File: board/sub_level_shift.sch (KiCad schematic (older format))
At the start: 17 parts, among them Q1501 Q_NPN_BEC, Q1502 Q_NPN_BEC, Q1503 Q_NPN_BEC, U1406 74LVC4245A, U1407 74LVC4245A, U1501 74LVC4245A, U1502 74LVC4245A, U1503 74LVC4245A, U1504 74LVC4245A, U1505 74LVC4245A

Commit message: More Schematic progress
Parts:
- added C1401, C1402, C1403, C1404, C1405, C1406, C1407: 1u, symbol Device:C
- renumbered Q1501 to Q1401, Q1502 to Q1402, Q1503 to Q1403, R1501 to R1401, R1502 to R1402, R1503 to R1403, R1504 to R1404, R1505 to R1405, R1506 to R1406, R1507 to R1407, U1406 to U1401, U1407 to U1402, U1501 to U1403, U1502 to U1404, U1503 to U1405, U1504 to U1406, U1505 to U1407
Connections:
- net +5V: now also C1401.1, C1402.1, C1403.1, C1404.1, C1405.1, C1406.1, C1407.1
- net A0: now also U1402.10 (A7), U1402.14 (B7); no longer U1401.21 (B0), U1401.3 (A0)
- net A1: now also U1402.15 (B6), U1402.9 (A6); no longer U1401.20 (B1), U1401.4 (A1)
- net A10: now also U1401.16 (B5), U1401.8 (A5); no longer U1402.19 (B2), U1402.5 (A2)
- net A11: now also U1401.17 (B4), U1401.7 (A4); no longer U1402.18 (B3), U1402.6 (A3)
- net A12: now also U1401.18 (B3), U1401.6 (A3); no longer U1402.17 (B4), U1402.7 (A4)
- net A13: now also U1401.19 (B2), U1401.5 (A2); no longer U1402.16 (B5), U1402.8 (A5)
- net A14: now also U1401.20 (B1), U1401.4 (A1); no longer U1402.15 (B6), U1402.9 (A6)
- net A15: now also U1401.21 (B0), U1401.3 (A0); no longer U1402.10 (A7), U1402.14 (B7)
- net A2: now also U1402.16 (B5), U1402.8 (A5); no longer U1401.19 (B2), U1401.5 (A2)
- net A3: now also U1402.17 (B4), U1402.7 (A4); no longer U1401.18 (B3), U1401.6 (A3)
- net A4: now also U1402.18 (B3), U1402.6 (A3); no longer U1401.17 (B4), U1401.7 (A4)
- net A5: now also U1402.19 (B2), U1402.5 (A2); no longer U1401.16 (B5), U1401.8 (A5)
- net A6: now also U1402.20 (B1), U1402.4 (A1); no longer U1401.15 (B6), U1401.9 (A6)
- net A7: now also U1402.21 (B0), U1402.3 (A0); no longer U1401.10 (A7), U1401.14 (B7)
- net A8: now also U1401.10 (A7), U1401.14 (B7); no longer U1402.21 (B0), U1402.3 (A0)
- net A9: now also U1401.15 (B6), U1401.9 (A6); no longer U1402.20 (B1), U1402.4 (A1)
- net GND: now also C1401.2, C1402.2, C1403.2, C1404.2, C1405.2, C1406.2, C1407.2
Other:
- moved on the sheet: Q1401, Q1402, Q1403, R1401, R1402, R1403, R1404, R1405, R1406, R1407, U1401, U1402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

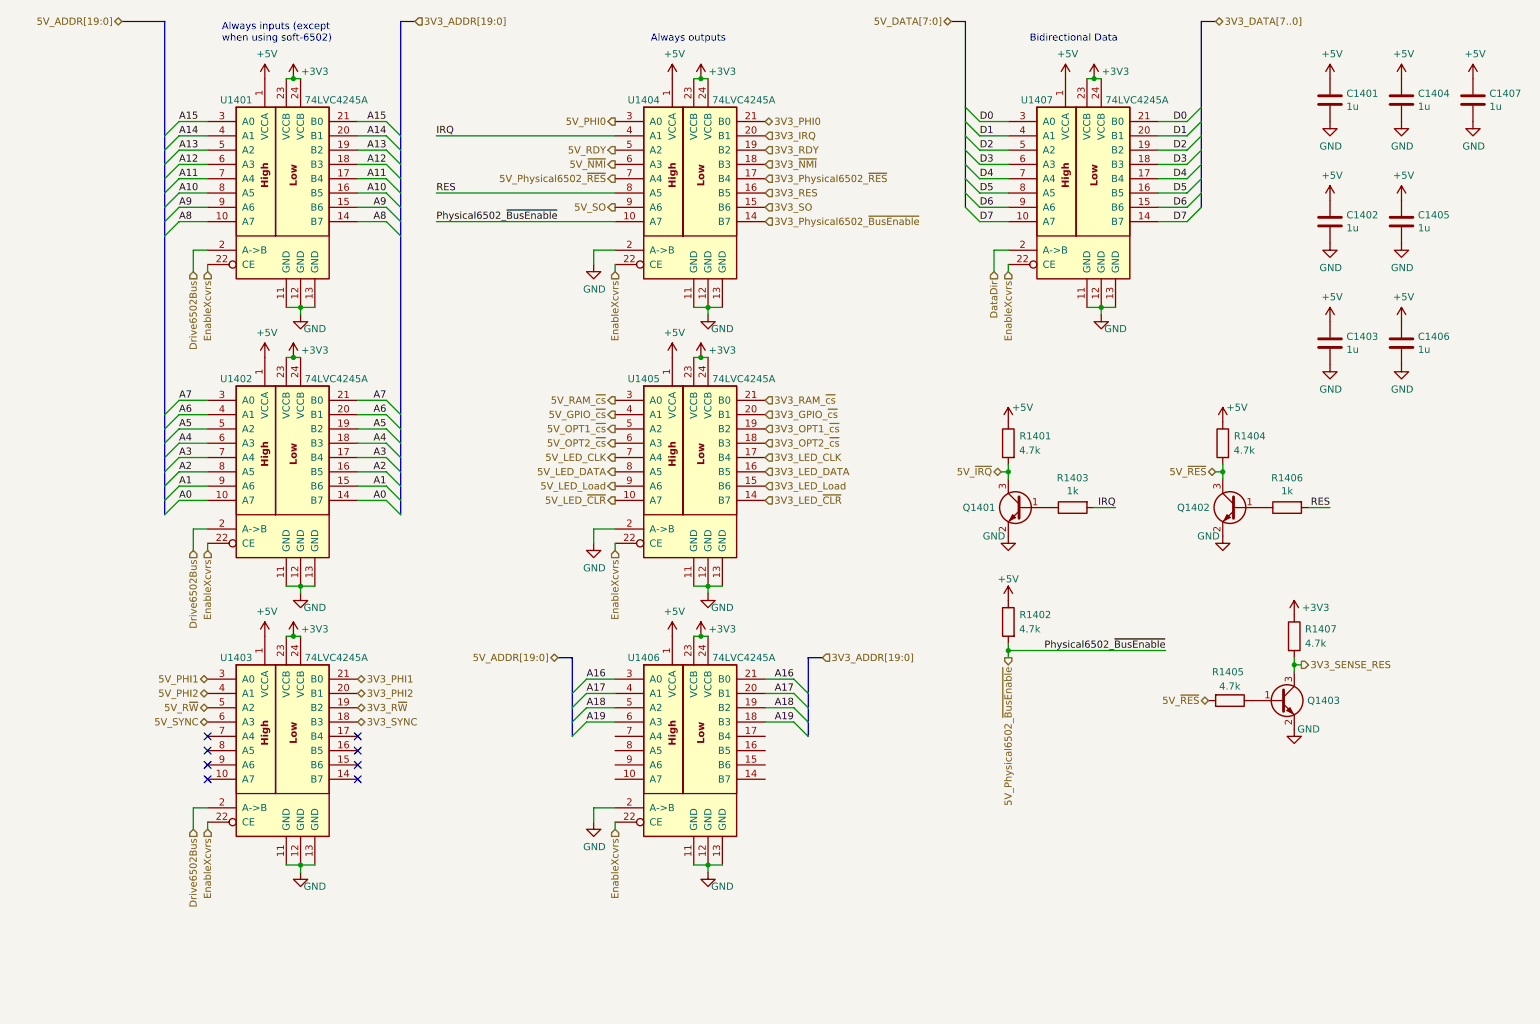
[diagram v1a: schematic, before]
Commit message: Bus signal connectivity rebuilt
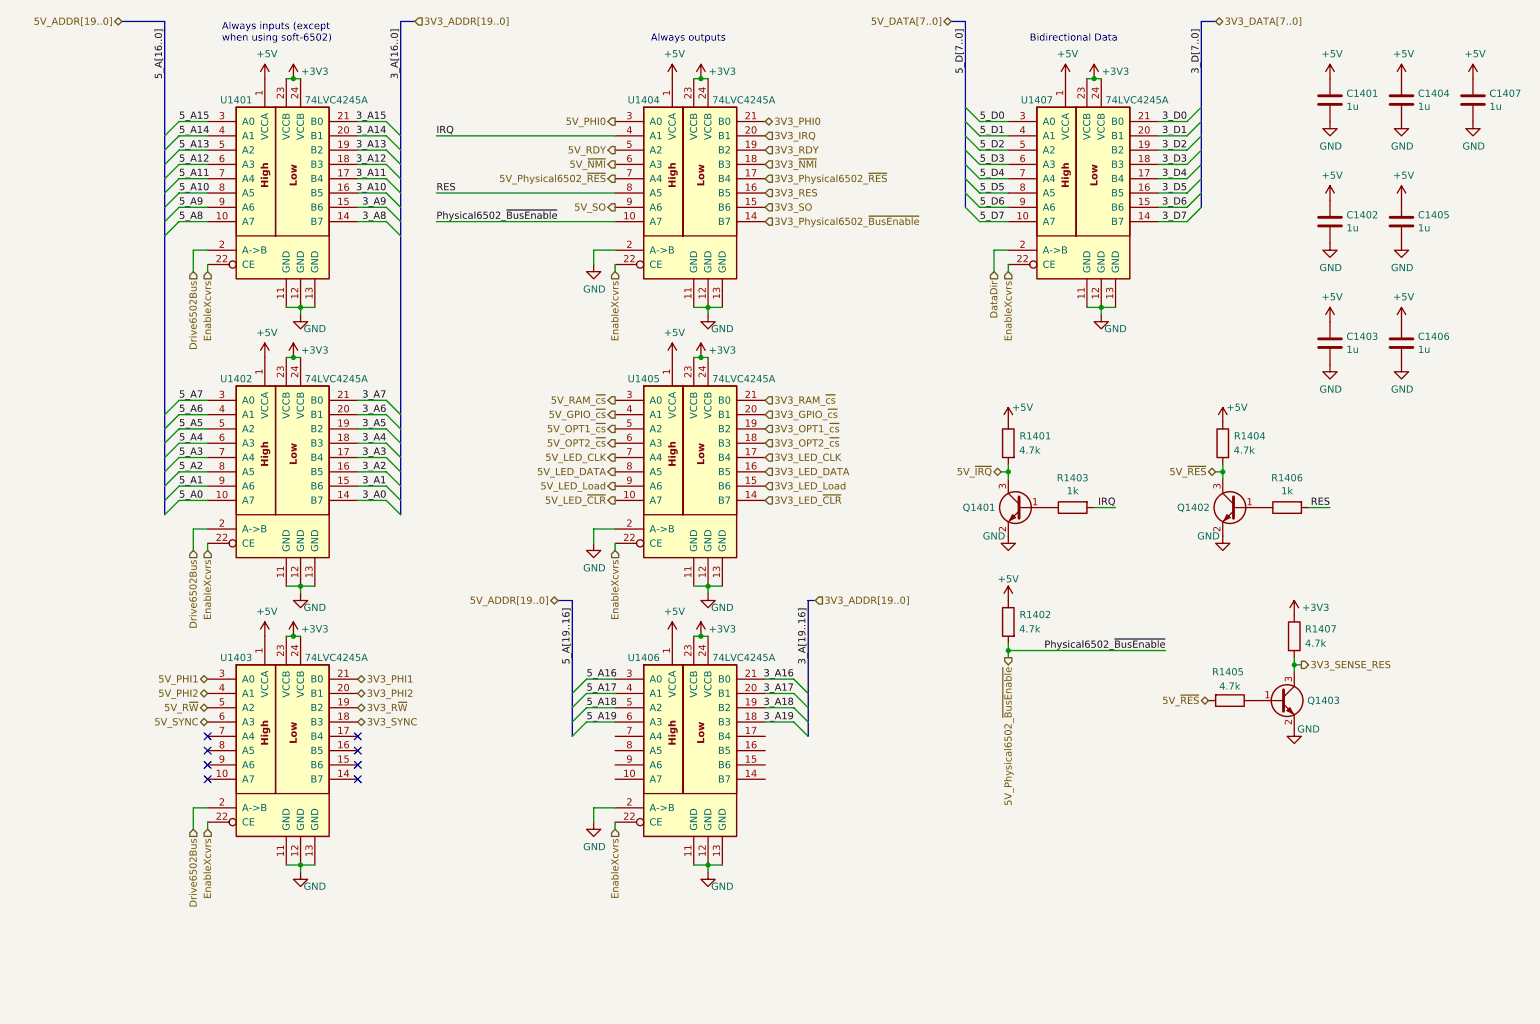
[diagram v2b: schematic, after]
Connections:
- net A0 renamed 3_A0
- net 3_A0: no longer U1402.10 (A7)
- net A1 renamed 3_A1
- net 3_A1: no longer U1402.9 (A6)
- net A10 renamed 3_A10
- net 3_A10: no longer U1401.8 (A5)
- net A11 renamed 3_A11
- net 3_A11: no longer U1401.7 (A4)
- net A12 renamed 3_A12
- net 3_A12: no longer U1401.6 (A3)
- net A13 renamed 3_A13
- net 3_A13: no longer U1401.5 (A2)
- net A14 renamed 3_A14
- net 3_A14: no longer U1401.4 (A1)
- net A15 renamed 3_A15
- net 3_A15: no longer U1401.3 (A0)
- net A16 renamed 3_A16
- net 3_A16: no longer U1406.3 (A0)
- net A17 renamed 3_A17
- net 3_A17: no longer U1406.4 (A1)
- net A18 renamed 3_A18
- net 3_A18: no longer U1406.5 (A2)
- net A19 renamed 3_A19
- net 3_A19: no longer U1406.6 (A3)
- net A2 renamed 3_A2
- net 3_A2: no longer U1402.8 (A5)
- net A3 renamed 3_A3
- net 3_A3: no longer U1402.7 (A4)
- net A4 renamed 3_A4
- net 3_A4: no longer U1402.6 (A3)
- net A5 renamed 3_A5
- net 3_A5: no longer U1402.5 (A2)
- net A6 renamed 3_A6
- net 3_A6: no longer U1402.4 (A1)
- net A7 renamed 3_A7
- net 3_A7: no longer U1402.3 (A0)
- net A8 renamed 3_A8
- net 3_A8: no longer U1401.10 (A7)
- net A9 renamed 3_A9
- net 3_A9: no longer U1401.9 (A6)
- net D0 renamed 3_D0
- net 3_D0: no longer U1407.3 (A0)
- net D1 renamed 3_D1
- net 3_D1: no longer U1407.4 (A1)
- net D2 renamed 3_D2
- net 3_D2: no longer U1407.5 (A2)
- net D3 renamed 3_D3
- net 3_D3: no longer U1407.6 (A3)
- net D4 renamed 3_D4
- net 3_D4: no longer U1407.7 (A4)
- net D5 renamed 3_D5
- net 3_D5: no longer U1407.8 (A5)
- net D6 renamed 3_D6
- net 3_D6: no longer U1407.9 (A6)
- net D7 renamed 3_D7
- net 3_D7: no longer U1407.10 (A7)
- new net 5_A0: U1402.10 (A7)
- new net 5_A1: U1402.9 (A6)
- new net 5_A10: U1401.8 (A5)
- new net 5_A11: U1401.7 (A4)
- new net 5_A12: U1401.6 (A3)
- new net 5_A13: U1401.5 (A2)
- new net 5_A14: U1401.4 (A1)
- new net 5_A15: U1401.3 (A0)
- new net 5_A16: U1406.3 (A0)
- new net 5_A17: U1406.4 (A1)
- new net 5_A18: U1406.5 (A2)
- new net 5_A19: U1406.6 (A3)
- new net 5_A2: U1402.8 (A5)
- new net 5_A3: U1402.7 (A4)
- new net 5_A4: U1402.6 (A3)
- new net 5_A5: U1402.5 (A2)
- new net 5_A6: U1402.4 (A1)
- new net 5_A7: U1402.3 (A0)
- new net 5_A8: U1401.10 (A7)
- new net 5_A9: U1401.9 (A6)
- new net 5_D0: U1407.3 (A0)
- new net 5_D1: U1407.4 (A1)
- new net 5_D2: U1407.5 (A2)
- new net 5_D3: U1407.6 (A3)
- new net 5_D4: U1407.7 (A4)
- new net 5_D5: U1407.8 (A5)
- new net 5_D6: U1407.9 (A6)
- new net 5_D7: U1407.10 (A7)
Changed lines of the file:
@@
 $EndDescr
 Text HLabel 6950 600  0    50   3State ~ 0
-5V_DATA[7:0]
+5V_DATA[7..0]
 Text HLabel 1150 600  0    50   BiDi ~ 0
-5V_ADDR[19:0]
+5V_ADDR[19..0]
 Text HLabel 1750 5400 0    50   BiDi ~ 0
 5V_R~W
@@
 Text HLabel 8800 600  2    50   3State ~ 0
 3V3_DATA[7..0]
-Text HLabel 6050 5050 2    50   Input ~ 0
-3V3_ADDR[19:0]
+Text HLabel 6000 4650 2    50   Input ~ 0
+3V3_ADDR[19..0]
 Text HLabel 2800 5400 2    50   BiDi ~ 0
 3V3_R~W
@@
 	1450 4050 1550 3950
 Text Label 1550 3950 0    50   ~ 0
-A0
+5_A0
 Text Label 1550 3850 0    50   ~ 0
-A1
+5_A1
 Text Label 1550 3750 0    50   ~ 0
-A2
+5_A2
 Text Label 1550 3650 0    50   ~ 0
-A3
+5_A3
 Text Label 1550 3550 0    50   ~ 0
-A4
+5_A4
 Text Label 1550 3450 0    50   ~ 0
-A5
+5_A5
 Text Label 1550 3350 0    50   ~ 0
-A6
+5_A6
 Text Label 1550 3250 0    50   ~ 0
-A7
+5_A7
 Text Label 3000 2000 2    50   ~ 0
-A8
+3_A8
 Text Label 3000 1900 2    50   ~ 0
-A9
+3_A9
 Text Label 3000 1800 2    50   ~ 0
-A10
+3_A10
 Text Label 3000 1700 2    50   ~ 0
-A11
+3_A11
 Text Label 3000 1300 2    50   ~ 0
-A15
+3_A15
 Text Label 3000 1400 2    50   ~ 0
-A14
+3_A14
 Text Label 3000 1500 2    50   ~ 0
-A13
+3_A13
 Text Label 3000 1600 2    50   ~ 0
-A12
+3_A12
 $Comp
 L power:GND #PWR01407
@@
 	7150 1300 7050 1200
 Text Label 7150 1300 0    50   ~ 0
-D0
+5_D0
 Text Label 7150 1400 0    50   ~ 0
-D1
+5_D1
 Text Label 7150 1500 0    50   ~ 0
-D2
+5_D2
 Text Label 7150 1600 0    50   ~ 0
-D3
+5_D3
 Text Label 7150 1700 0    50   ~ 0
-D4
+5_D4
 Text Label 7150 1800 0    50   ~ 0
-D5
+5_D5
 Text Label 7150 1900 0    50   ~ 0
-D6
+5_D6
 Text Label 7150 2000 0    50   ~ 0
-D7
+5_D7
 Wire Wire Line
 	7350 2000 7150 2000
@@
 	4450 6100 4600 6100
 Text HLabel 3200 600  2    50   Input ~ 0
-3V3_ADDR[19:0]
+3V3_ADDR[19..0]
 Wire Bus Line
 	6950 600  7050 600
@@
 	8600 1300 8700 1200
 Text Label 8600 1300 2    50   ~ 0
-D0
+3_D0
 Text Label 8600 1400 2    50   ~ 0
-D1
+3_D1
 Text Label 8600 1500 2    50   ~ 0
-D2
+3_D2
 Text Label 8600 1600 2    50   ~ 0
-D3
+3_D3
 Text Label 8600 1700 2    50   ~ 0
-D4
+3_D4
 Text Label 8600 1800 2    50   ~ 0
-D5
+3_D5
 Text Label 8600 1900 2    50   ~ 0
-D6
+3_D6
 Text Label 8600 2000 2    50   ~ 0
-D7
+3_D7
 Wire Wire Line
 	8400 2000 8600 2000
@@
 	4300 5600 4400 5500
 Text Label 4400 5500 0    50   ~ 0
-A19
+5_A19
 Text Label 4400 5400 0    50   ~ 0
-A18
+5_A18
 Text Label 4400 5300 0    50   ~ 0
-A17
+5_A17
 Text Label 4400 5200 0    50   ~ 0
-A16
+5_A16
 Wire Wire Line
 	4400 5500 4600 5500
@@
 	4600 5200 4400 5200
 Wire Bus Line
-	4300 5050 4200 5050
+	4300 4650 4200 4650
 Entry Wire Line
 	5950 5300 5850 5200
@@
 	5950 5600 5850 5500
 Text Label 5850 5500 2    50   ~ 0
-A19
+3_A19
 Text Label 5850 5400 2    50   ~ 0
-A18
+3_A18
 Text Label 5850 5300 2    50   ~ 0
-A17
+3_A17
 Text Label 5850 5200 2    50   ~ 0
-A16
+3_A16
 Wire Wire Line
 	5850 5500 5650 5500
@@
 	5650 5200 5850 5200
 Wire Bus Line
-	5950 5050 6050 5050
-Text HLabel 4200 5050 0    50   BiDi ~ 0
-5V_ADDR[19:0]
+	5950 4650 6000 4650
+Text HLabel 4200 4650 0    50   BiDi ~ 0
+5V_ADDR[19..0]
 Wire Wire Line
 	8100 2600 8000 2600
@@
 $EndComp
 Text Label 1550 2000 0    50   ~ 0
-A8
+5_A8
 Text Label 1550 1900 0    50   ~ 0
-A9
+5_A9
 Text Label 1550 1800 0    50   ~ 0
-A10
+5_A10
 Text Label 1550 1700 0    50   ~ 0
-A11
+5_A11
 Text Label 1550 1300 0    50   ~ 0
-A15
+5_A15
 Text Label 1550 1400 0    50   ~ 0
-A14
+5_A14
 Text Label 1550 1500 0    50   ~ 0
-A13
+5_A13
 Text Label 1550 1600 0    50   ~ 0
-A12
+5_A12
 Text Label 3000 3950 2    50   ~ 0
-A0
+3_A0
 Text Label 3000 3850 2    50   ~ 0
-A1
+3_A1
 Text Label 3000 3750 2    50   ~ 0
-A2
+3_A2
 Text Label 3000 3650 2    50   ~ 0
-A3
+3_A3
 Text Label 3000 3550 2    50   ~ 0
-A4
+3_A4
 Text Label 3000 3450 2    50   ~ 0
-A5
+3_A5
 Text Label 3000 3350 2    50   ~ 0
-A6
+3_A6
 Text Label 3000 3250 2    50   ~ 0
-A7
+3_A7
 Wire Wire Line
 	1550 1300 1750 1300
@@
 Wire Wire Line
 	1550 3950 1750 3950
+Text Label 8700 650  3    50   ~ 0
+3_D[7..0]
+Text Label 7050 650  3    50   ~ 0
+5_D[7..0]
+Text Label 1450 650  3    50   ~ 0
+5_A[16..0]
+Text Label 3100 650  3    50   ~ 0
+3_A[16..0]
+Text Label 5950 4700 3    50   ~ 0
+3_A[19..16]
 Wire Bus Line
-	5950 5050 5950 5600
+	5950 4650 5950 5600
 Wire Bus Line
-	4300 5050 4300 5600
+	4300 4650 4300 5600
 Wire Bus Line
 	8700 600  8700 1900
@@
 Wire Bus Line
 	1450 600  1450 4050
+Text Label 4300 4700 3    50   ~ 0
+5_A[19..16]
 $EndSCHEMATC

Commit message: gpio done
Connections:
- net 3V3_GPIO_~cs is gone; now on net 3V3_OPT1_~cs: U1405.20 (B1)
- net 5V_GPIO_~cs is gone; now on net 5V_OPT1_~cs: U1405.4 (A1)
- net 3V3_LED_CLK: now also U1405.18 (B3); no longer U1405.17 (B4)
- net 3V3_LED_DATA: now also U1405.17 (B4); no longer U1405.16 (B5)
- net 3V3_LED_Load: now also U1405.16 (B5); no longer U1405.15 (B6)
- net 3V3_LED_~CLR: now also U1405.15 (B6); no longer U1405.14 (B7)
- net 3V3_OPT1_~cs: no longer U1405.19 (B2)
- net 3V3_OPT2_~cs: now also U1405.19 (B2); no longer U1405.18 (B3)
- net 5V_LED_CLK: now also U1405.6 (A3); no longer U1405.7 (A4)
- net 5V_LED_DATA: now also U1405.7 (A4); no longer U1405.8 (A5)
- net 5V_LED_Load: now also U1405.8 (A5); no longer U1405.9 (A6)
- net 5V_LED_~CLR: now also U1405.9 (A6); no longer U1405.10 (A7)
- net 5V_OPT1_~cs: no longer U1405.5 (A2)
- net 5V_OPT2_~cs: now also U1405.5 (A2); no longer U1405.6 (A3)
- no-connect marks 8 -> 10
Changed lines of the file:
@@
 5V_RAM_~cs
 Text HLabel 4600 3350 0    50   Output ~ 0
-5V_GPIO_~cs
+5V_OPT1_~cs
 Text HLabel 4600 3450 0    50   Output ~ 0
-5V_OPT1_~cs
-Text HLabel 4600 3550 0    50   Output ~ 0
 5V_OPT2_~cs
 Text HLabel 1750 5500 0    50   BiDi ~ 0
@@
 3V3_RAM_~cs
 Text HLabel 5650 3350 2    50   Input ~ 0
-3V3_GPIO_~cs
+3V3_OPT1_~cs
 Text HLabel 5650 3450 2    50   Input ~ 0
-3V3_OPT1_~cs
-Text HLabel 5650 3550 2    50   Input ~ 0
 3V3_OPT2_~cs
 Text HLabel 2800 5500 2    50   BiDi ~ 0
@@
 Wire Wire Line
 	4450 4150 4600 4150
+Text HLabel 4600 3550 0    50   Output ~ 0
+5V_LED_CLK
 Text HLabel 4600 3650 0    50   Output ~ 0
-5V_LED_CLK
+5V_LED_DATA
 Text HLabel 4600 3750 0    50   Output ~ 0
-5V_LED_DATA
-Text HLabel 4600 3850 0    50   Output ~ 0
 5V_LED_Load
 $Comp
@@
 Wire Wire Line
 	7250 2200 7350 2200
+Text HLabel 5650 3550 2    50   Input ~ 0
+3V3_LED_CLK
 Text HLabel 5650 3650 2    50   Input ~ 0
-3V3_LED_CLK
+3V3_LED_DATA
 Text HLabel 5650 3750 2    50   Input ~ 0
-3V3_LED_DATA
+3V3_LED_Load
 Text HLabel 5650 3850 2    50   Input ~ 0
-3V3_LED_Load
-Text HLabel 5650 3950 2    50   Input ~ 0
 3V3_LED_~CLR
-Text HLabel 4600 3950 0    50   Output ~ 0
+Text HLabel 4600 3850 0    50   Output ~ 0
 5V_LED_~CLR
 Wire Wire Line
@@
 Text Label 5950 4700 3    50   ~ 0
 3_A[19..16]
+Text Label 4300 4700 3    50   ~ 0
+5_A[19..16]
+NoConn ~ 5650 3950
+NoConn ~ 4600 3950
 Wire Bus Line
 	5950 4650 5950 5600
@@
 Wire Bus Line
 	1450 600  1450 4050
-Text Label 4300 4700 3    50   ~ 0
-5_A[19..16]
 $EndSCHEMATC
